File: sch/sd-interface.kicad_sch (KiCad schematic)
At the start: 34 parts, among them J15 F32Q-1A7H1-11022, J16 MEM2075-00-140-01-A, J17 3V5_out, Q1 Q_PMOS_GSD, U10 CD4043BDR, U11 TPS22919DCKR, U8 MAX4996LETG_

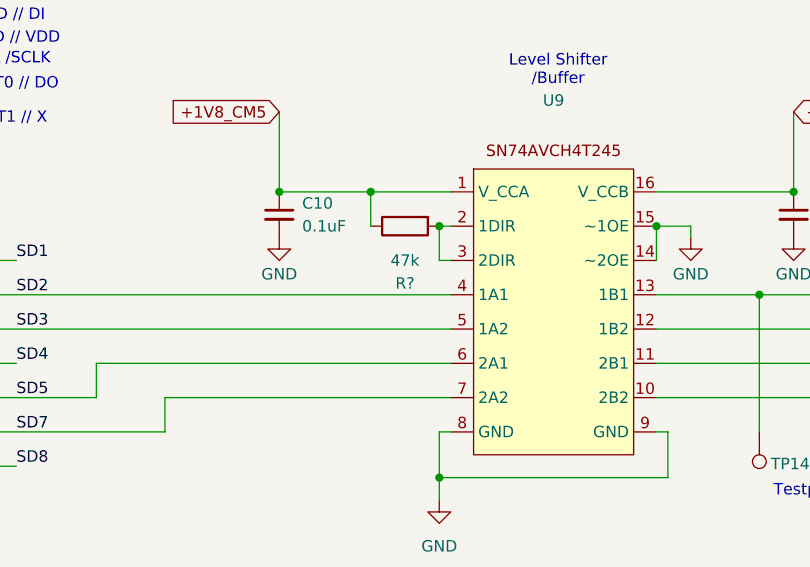
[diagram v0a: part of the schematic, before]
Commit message: Ferdig pcb-layout modem og simkort, ikke kobla til CM enda
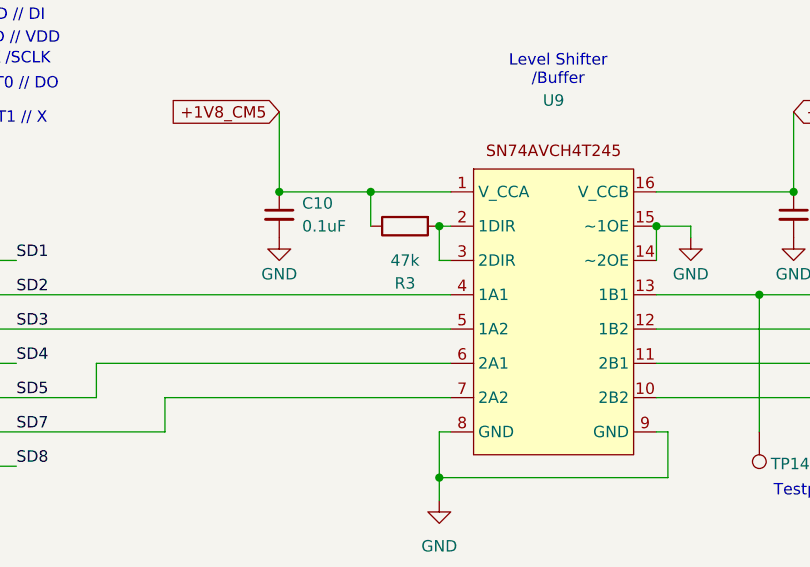
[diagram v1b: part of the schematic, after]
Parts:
- gave numbers to parts that had none: 1
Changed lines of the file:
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@@
 		(on_board yes)
 		(dnp no)
-		(property "Reference" "R?"
+		(property "Reference" "R3"
 			(at 179.07 53.34 90)
 			(effects
@@
 			(project "audiograb"
 				(path "/c46c2311-6d4b-411d-b012-c7730eac136d/6c55ccce-577d-49c2-8294-3a5d8e11981e"
-					(reference "R?")
+					(reference "R3")
 					(unit 1)
 				)

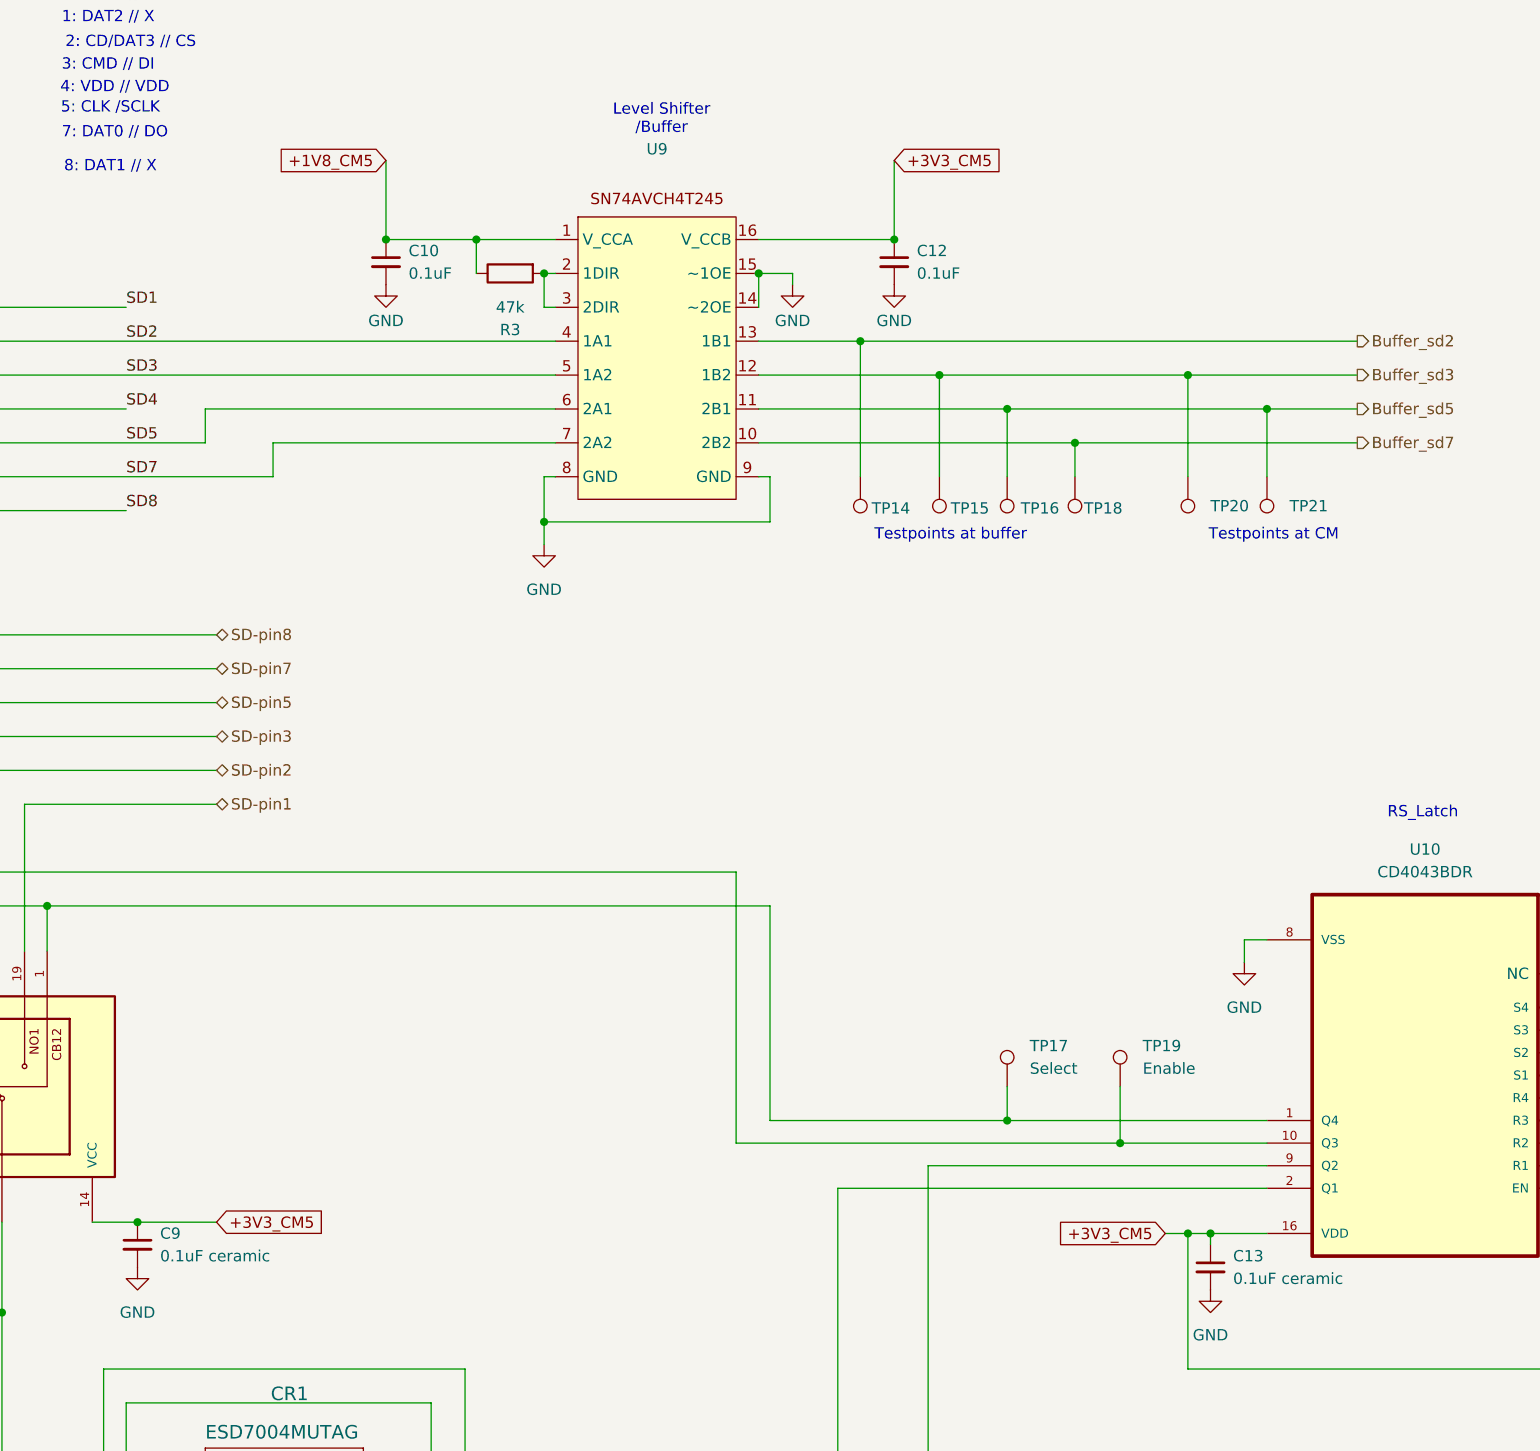
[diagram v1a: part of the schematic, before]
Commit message: partnumber, manufaturerer and description cleanup completed
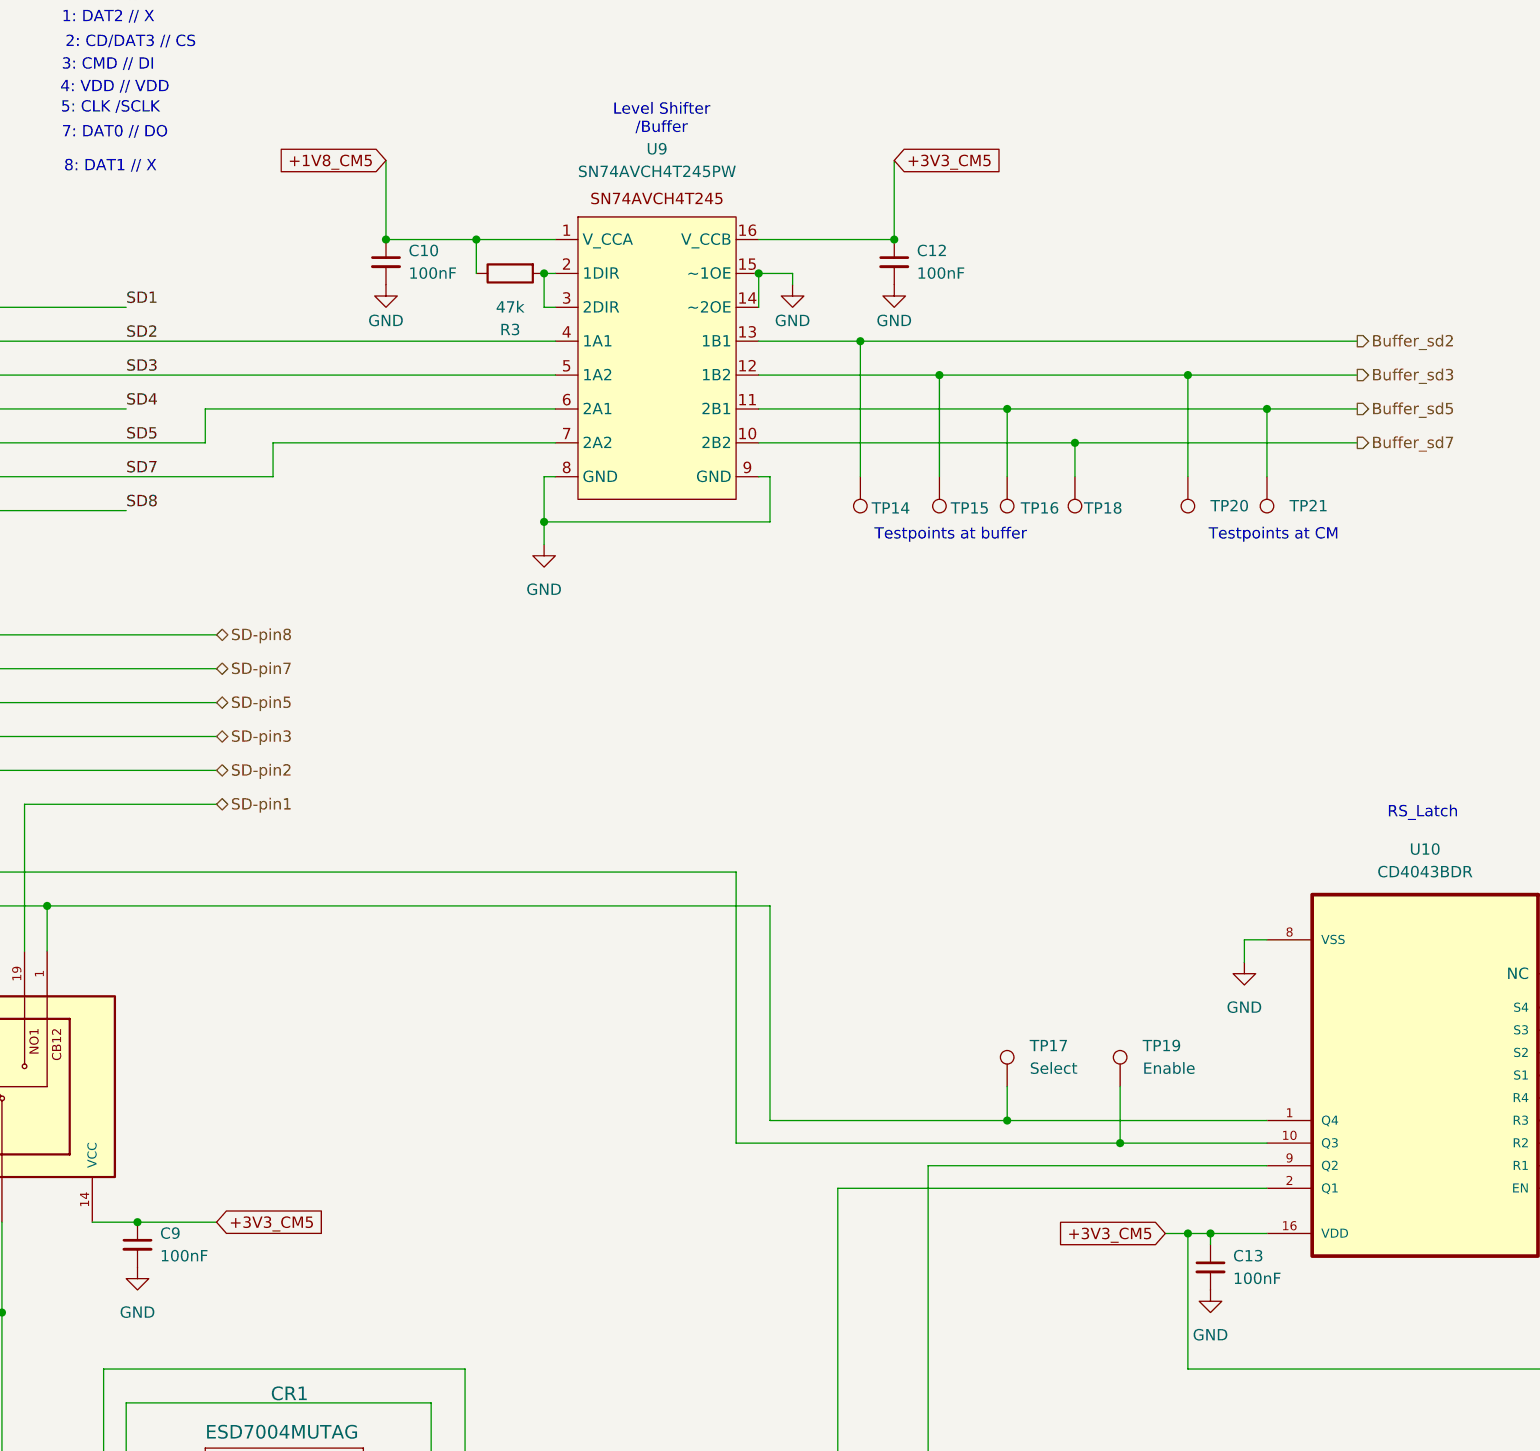
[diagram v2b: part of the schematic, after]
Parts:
- C10, C12: value 0.1uF -> 100nF
- C13, C9: value 0.1uF ceramic -> 100nF
- CR1, CR2: MPN (none) -> ESD7004MUTAG
- J15: Description_1 Flex Connector, 0.50mm Pitch, Height 2.00mm, Right angle, S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 -> (none); MANUFACTURER Amphenol -> (none); MP F32Q-1A7H1-11022 -> (none); MPN (none) -> F32Q-1A7H1-11022; Manufacturer (none) -> Amphenol
- J16: Description_1 9 (8 + 1) Position Card Connector microSD Surface Mount, Ri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 -> (none); MANUFACTURER GCT -> (none); MP MEM2075-00-140-01-A -> (none); MPN (none) -> MEM2075-00-140-01-A; Manufacturer (none) -> GCT
- J17: Description_1 2 Position Wire to Board Terminal Block Horizontal with Boa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 -> (none); MF Würth Elektronik -> (none); MP 691137710002 -> (none); MPN (none) -> 691137710002; Manufacturer (none) -> Würth Elektronik
- Q1: MPN (none) -> SSM3K333R,LF
- U10: Description_1 CMOS Quad NOR R/S Latch with 3-State Outputs -> (none); MF Texas Instruments -> (none); MP CD4043BDR -> (none); MPN (none) -> CD4043BDR; Manufacturer (none) -> Texas Instruments
- U11: Description_1 5.5-V, 1.5-A, 90-mΩ load switch with adj. output discharge -> (none); MF Texas Instruments -> (none); MP TPS22919DCKR -> (none); MPN (none) -> TPS22919DCKR; Manufacturer (none) -> Texas Instruments
- U8: Description_1 Triple DPDT, Low-Capacitance Data Switches -> (none); MANUFACTURER MAXIM INTEGRATED -> (none); MP MAX4996LETG+ -> (none); MPN (none) -> MAX4996LETG+; Manufacturer (none) -> Analog Devices Inc./Maxim Integrated
- U9: value ~ -> SN74AVCH4T245PW; MP SN74AVCH4T245PW -> (none); MPN (none) -> SN74AVCH4T245PW
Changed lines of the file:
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@@
 			)
 		)
-		(property "Description" ""
+		(property "Description" "ESD Protection Diodes / TVS Diodes Low Capacitance ESD Protection Diode"
+			(at 137.16 231.14 0)
+			(effects
+				(font
+					(size 1.27 1.27)
+				)
+				(hide yes)
+			)
+		)
+		(property "MPN" "ESD7004MUTAG"
 			(at 137.16 231.14 0)
 			(effects
@@
 			)
 		)
-		(property "Value" "0.1uF"
+		(property "Value" "100nF"
 			(at 167.64 46.9962 0)
 			(effects
@@
 			)
 		)
-		(property "Description" "5V power out"
-			(at 354.33 218.44 0)
-			(effects
-				(font
-					(size 1.27 1.27)
-				)
-				(hide yes)
-			)
-		)
-		(property "MF" "Würth Elektronik"
+		(property "Description" "2 Position Wire to Board Terminal Block Horizontal with Board 0.197 (5.00mm) Through Hole"
 			(at 354.33 218.44 0)
 			(effects
@@
 					(size 1.27 1.27)
 				)
-				(justify bottom)
 				(hide yes)
 			)
 		)
-		(property "Description_1" "2 Position Wire to Board Terminal Block Horizontal with Board 0.197 (5.00mm) Through Hole"
+		(property "Manufacturer" "Würth Elektronik"
 			(at 354.33 218.44 0)
 			(effects
@@
 			)
 		)
-		(property "MP" "691137710002"
+		(property "MPN" "691137710002"
 			(at 354.33 218.44 0)
 			(effects
@@
 			)
 		)
-		(property "Value" "0.1uF ceramic"
+		(property "Value" "100nF"
 			(at 139.7 157.4862 0)
 			(effects
@@
 			)
 		)
-		(property "Description" ""
+		(property "Description" "9 (8 + 1) Position Card Connector microSD Surface Mount, Right Angle Gold"
 			(at 157.48 266.7 0)
 			(effects
@@
 			)
 		)
-		(property "Description_1" "9 (8 + 1) Position Card Connector microSD Surface Mount, Right Angle Gold"
-			(at 157.48 266.7 0)
-			(effects
-				(font
-					(size 1.27 1.27)
-				)
-				(justify bottom)
-				(hide yes)
-			)
-		)
 		(property "Package" "None"
 			(at 157.48 266.7 0)
@@
 			)
 		)
-		(property "MP" "MEM2075-00-140-01-A"
+		(property "MPN" "MEM2075-00-140-01-A"
 			(at 157.48 266.7 0)
 			(effects
@@
 			)
 		)
-		(property "MANUFACTURER" "GCT"
+		(property "Manufacturer" "GCT"
 			(at 157.48 266.7 0)
 			(effects
@@
 			)
 		)
-		(property "Value" "~"
+		(property "Value" "SN74AVCH4T245PW"
 			(at 195.58 35.56 0)
 			(effects
@@
 			)
 		)
-		(property "Description" ""
+		(property "Description" "Translation - Voltage Levels 4-Bit Dual-Supply Bu s Xcvr A 595-SN74AV A 595-SN74AVCH4T245PWT"
 			(at 195.58 57.15 0)
 			(effects
@@
 			)
 		)
-		(property "MP" "SN74AVCH4T245PW"
+		(property "MPN" "SN74AVCH4T245PW"
 			(at 195.58 57.15 0)
 			(effects
@@
 			)
 		)
-		(property "Description" ""
+		(property "Description" "5.5-V, 1.5-A, 90-mΩ load switch with adj. output discharge"
 			(at 297.18 220.98 0)
 			(effects
@@
 			)
 		)
-		(property "MF" "Texas Instruments"
-			(at 297.18 220.98 0)
-			(effects
-				(font
-					(size 1.27 1.27)
-				)
-				(justify bottom)
-				(hide yes)
-			)
-		)
-		(property "Description_1" "5.5-V, 1.5-A, 90-mΩ load switch with adj. output discharge"
+		(property "Manufacturer" "Texas Instruments"
 			(at 297.18 220.98 0)
 			(effects
@@
 			)
 		)
-		(property "MP" "TPS22919DCKR"
+		(property "MPN" "TPS22919DCKR"
 			(at 297.18 220.98 0)
 			(effects
@@
 			)
 		)
-		(property "Description" ""
+		(property "Description" "ESD Protection Diodes / TVS Diodes Low Capacitance ESD Protection Diode"
+			(at 137.16 186.69 0)
+			(effects
+				(font
+					(size 1.27 1.27)
+				)
+				(hide yes)
+			)
+		)
+		(property "MPN" "ESD7004MUTAG"
 			(at 137.16 186.69 0)
 			(effects
@@
 			)
 		)
-		(property "Description" ""
+		(property "Description" "Flex Connector, 0.50mm Pitch, Height 2.00mm, Right angle, Slider type, ZIF, Upper contact, 22 position , Without MYLAR"
 			(at 88.9 26.67 0)
 			(effects
@@
 			)
 		)
-		(property "MP" "F32Q-1A7H1-11022"
-			(at 88.9 26.67 0)
-			(effects
-				(font
-					(size 1.27 1.27)
-				)
-				(justify bottom)
-				(hide yes)
-			)
-		)
-		(property "Description_1" "Flex Connector, 0.50mm Pitch, Height 2.00mm, Right angle, Slider type, ZIF, Upper contact, 22 position , Without MYLAR"
+		(property "MPN" "F32Q-1A7H1-11022"
 			(at 88.9 26.67 0)
 			(effects
@@
 			)
 		)
-		(property "MANUFACTURER" "Amphenol"
+		(property "Manufacturer" "Amphenol"
 			(at 88.9 26.67 0)
 			(effects
@@
 			)
 		)
+		(property "MPN" "SSM3K333R,LF "
+			(at 199.39 245.11 0)
+			(effects
+				(font
+					(size 1.27 1.27)
+				)
+				(hide yes)
+			)
+		)
 		(pin "2"
 		)
@@
 			)
 		)
-		(property "Description" ""
-			(at 281.94 137.16 0)
-			(effects
-				(font
-					(size 1.27 1.27)
-				)
-				(hide yes)
-			)
-		)
-		(property "MF" "Texas Instruments"
+		(property "Description" "CMOS Quad NOR R/S Latch with 3-State Outputs"
 			(at 281.94 137.16 0)
 			(effects
@@
 					(size 1.27 1.27)
 				)
-				(justify bottom)
 				(hide yes)
 			)
 		)
-		(property "Description_1" "CMOS Quad NOR R/S Latch with 3-State Outputs"
+		(property "Manufacturer" "Texas Instruments"
 			(at 281.94 137.16 0)
 			(effects
@@
 			)
 		)
-		(property "MP" "CD4043BDR"
+		(property "MPN" "CD4043BDR"
 			(at 281.94 137.16 0)
 			(effects
@@
 			)
 		)
-		(property "Description" ""
+		(property "Description" "Triple DPDT, Low-Capacitance Data Switches"
 			(at 93.98 138.43 0)
 			(effects
@@
 			)
 		)
-		(property "Description_1" "Triple DPDT, Low-Capacitance Data Switches"
-			(at 93.98 138.43 0)
-			(effects
-				(font
-					(size 1.27 1.27)
-				)
-				(justify bottom)
-				(hide yes)
-			)
-		)
 		(property "Package" "TQFN-24 Maxim"
 			(at 93.98 138.43 0)
@@
 			)
 		)
-		(property "MP" "MAX4996LETG+"
+		(property "MPN" "MAX4996LETG+"
 			(at 93.98 138.43 0)
 			(effects
@@
 			)
 		)
-		(property "MANUFACTURER" "MAXIM INTEGRATED"
+		(property "Manufacturer" "Analog Devices Inc./Maxim Integrated"
 			(at 93.98 138.43 0)
 			(effects
@@
 			)
 		)
-		(property "Value" "0.1uF ceramic"
+		(property "Value" "100nF"
 			(at 260.35 160.0262 0)
 			(effects
@@
 			)
 		)
-		(property "Value" "0.1uF"
+		(property "Value" "100nF"
 			(at 224.79 46.9962 0)
 			(effects
